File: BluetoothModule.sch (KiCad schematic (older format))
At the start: 13 parts, among them U2 BM83SM1-00TA

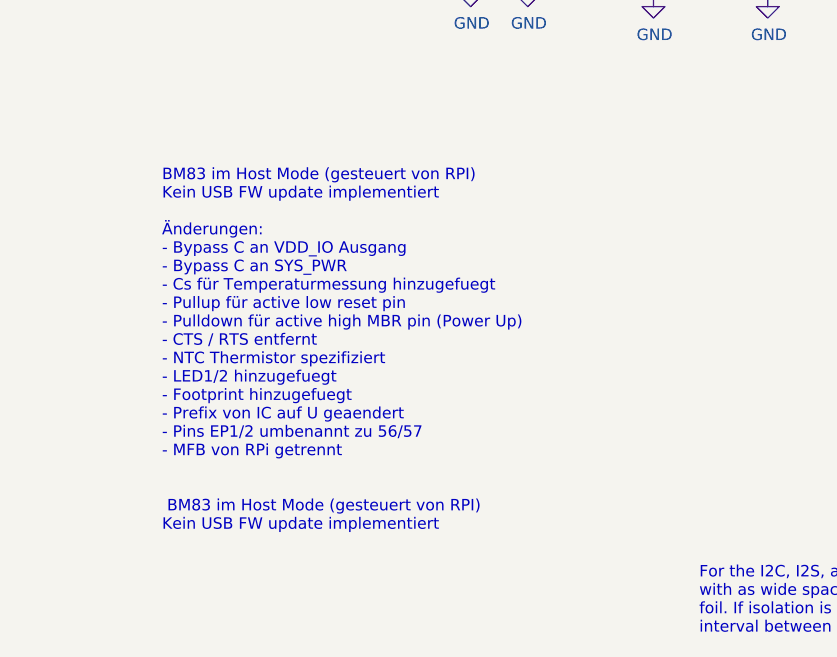
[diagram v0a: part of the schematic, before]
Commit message: - Erster Stand UI Board Layout
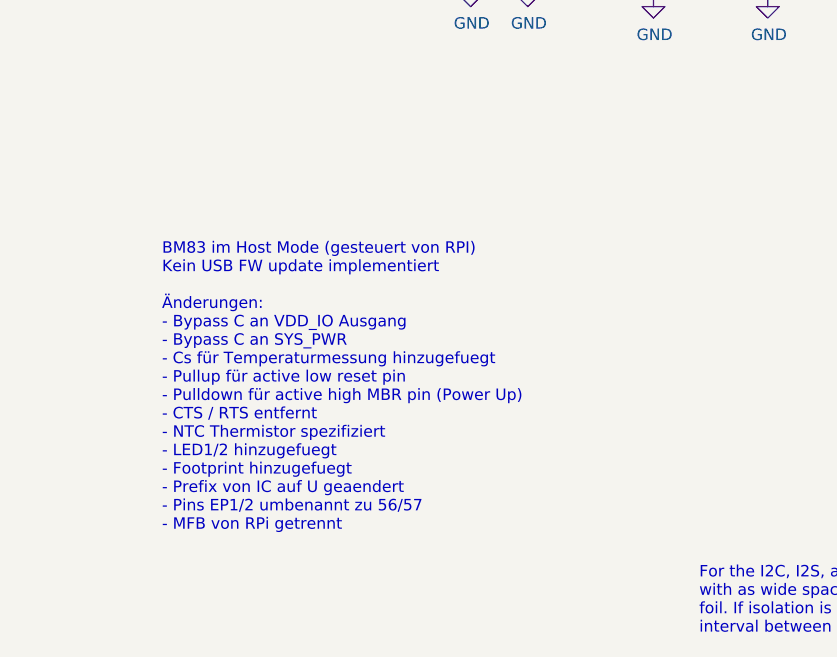
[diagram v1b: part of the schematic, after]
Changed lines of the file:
@@
 	6600 3850 6600 3950
 Text Notes 1050 7150 0    50   ~ 0
-BM83 im Host Mode (gesteuert von RPI)\nKein USB FW update implementiert\n\nÄnderungen:\n- Bypass C an VDD_IO Ausgang\n- Bypass C an SYS_PWR\n- Cs für Temperaturmessung hinzugefuegt\n- Pullup für active low reset pin\n- Pulldown für active high MBR pin (Power Up)\n- CTS / RTS entfernt\n- NTC Thermistor spezifiziert\n- LED1/2 hinzugefuegt\n- Footprint hinzugefuegt\n- Prefix von IC auf U geaendert\n- Pins EP1/2 umbenannt zu 56/57 \n- MFB von RPi getrennt\n\n\n BM83 im Host Mode (gesteuert von RPI)\nKein USB FW update implementiert
+BM83 im Host Mode (gesteuert von RPI)\nKein USB FW update implementiert\n\nÄnderungen:\n- Bypass C an VDD_IO Ausgang\n- Bypass C an SYS_PWR\n- Cs für Temperaturmessung hinzugefuegt\n- Pullup für active low reset pin\n- Pulldown für active high MBR pin (Power Up)\n- CTS / RTS entfernt\n- NTC Thermistor spezifiziert\n- LED1/2 hinzugefuegt\n- Footprint hinzugefuegt\n- Prefix von IC auf U geaendert\n- Pins EP1/2 umbenannt zu 56/57 \n- MFB von RPi getrennt
 $Bitmap
 Pos 5150 6250

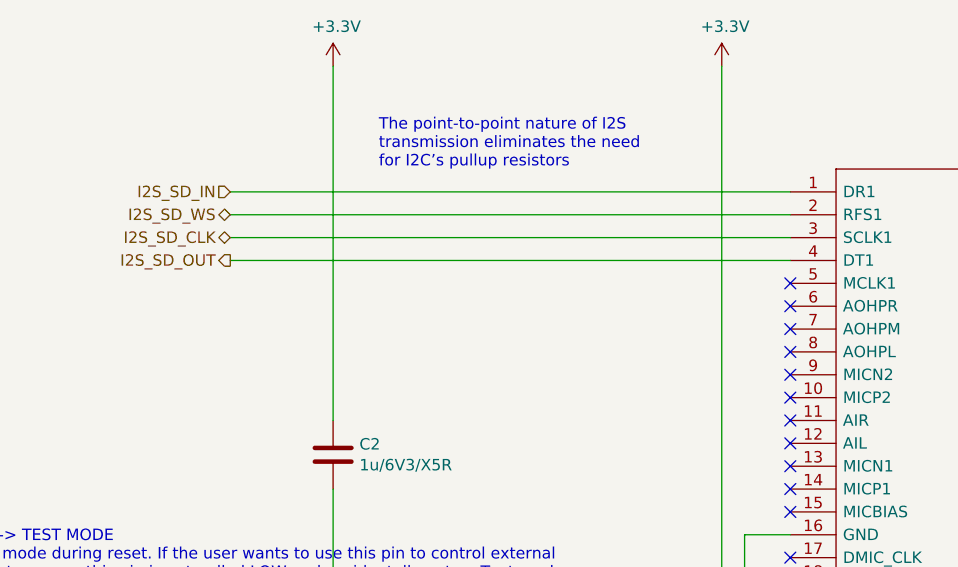
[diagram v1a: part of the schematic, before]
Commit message: [mod:] MCLK input to MAX98089 from BM83 at 12.28MHz
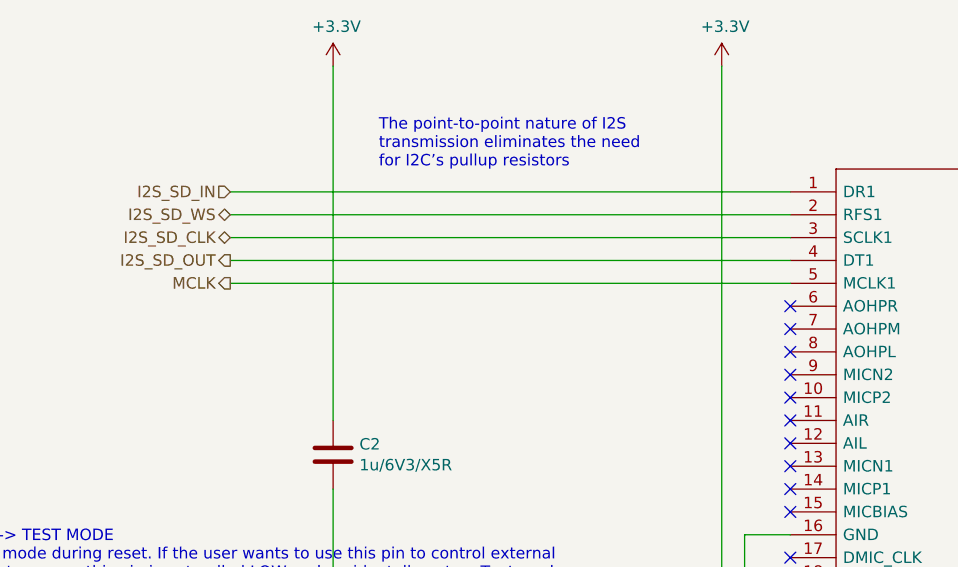
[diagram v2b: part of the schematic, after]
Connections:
- net MCLK: now reaches U2.5 (MCLK1)
- no-connect marks 34 -> 33
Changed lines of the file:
@@
 Text Notes 3400 7600 0    50   ~ 0
 For the I2C, I2S, and UART groups, each respective group's traces should run parallel\nwith as wide spacing as possible and be isolated from other groups with GND copper\nfoil. If isolation is not possible due to limited space, please at least increase the \ninterval between traces belonging to different groups.
-NoConn ~ 4400 1850
 Text Notes 7000 6350 0    50   ~ 0
 Wird das Modul als I2S Master betrieben, kann dessen MCLK Ausgang zur Frequenzversorgung \ndes Slaves verwendet werden. Dies ist hier aber nicht der Fall, daher bleibt MCLK unbeschalten.\nvgl. DS 6.5. Vermutlich könnte das Modul den MAX98089 mit dem Takt versorgen, \nso dass der Oszillator für MAX98 entfallen kann\n\nThe BM83 serves as a master to provide clock and frame synchronous signals for the master/slave data\nsynchronizations, as illustrated in the following figures. The MCLK is optional and is not required if the\nexternal I2S device can drive its system clock on its own.\n\nMaster CLK is not part of the I2S standard, but is commonly included for synchronizing \nthe internal operation of the analog/digital converters.\nQuelle: https://en.wikipedia.org/wiki/I%C2%B2S
@@
 	1    0    0    -1
 $EndComp
+Text HLabel 1950 1850 0    50   Output ~ 0
+MCLK
+Wire Wire Line
+	1950 1850 4400 1850
 $EndSCHEMATC

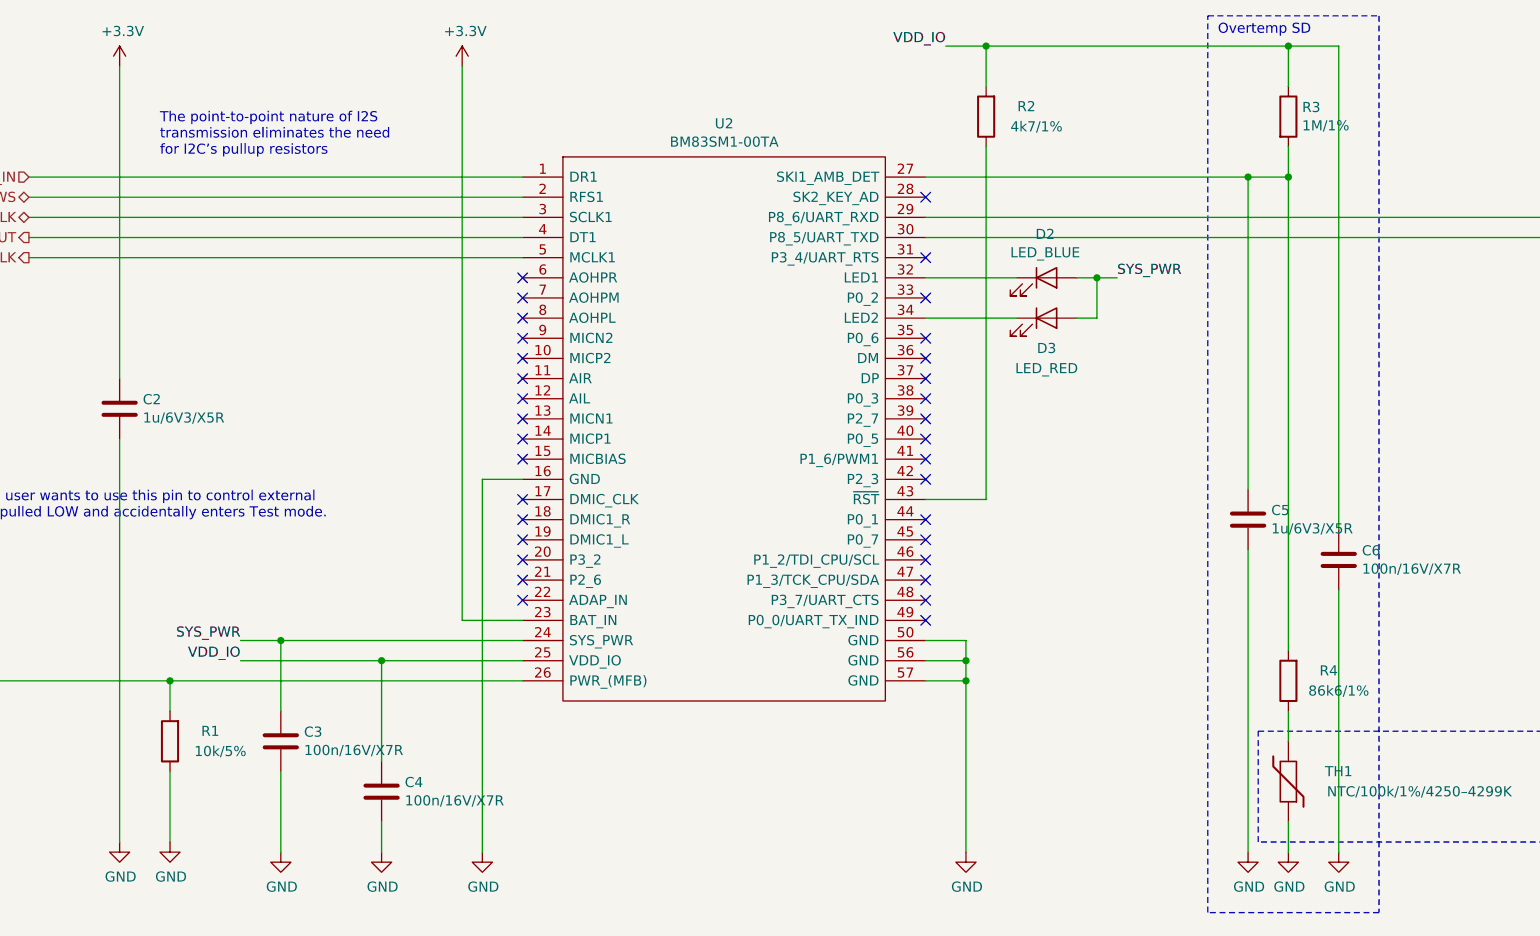
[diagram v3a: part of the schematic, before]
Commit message: - Schaltbare BL Versorgung fertig - kleinere Value Anpassungen - Finale Annotation
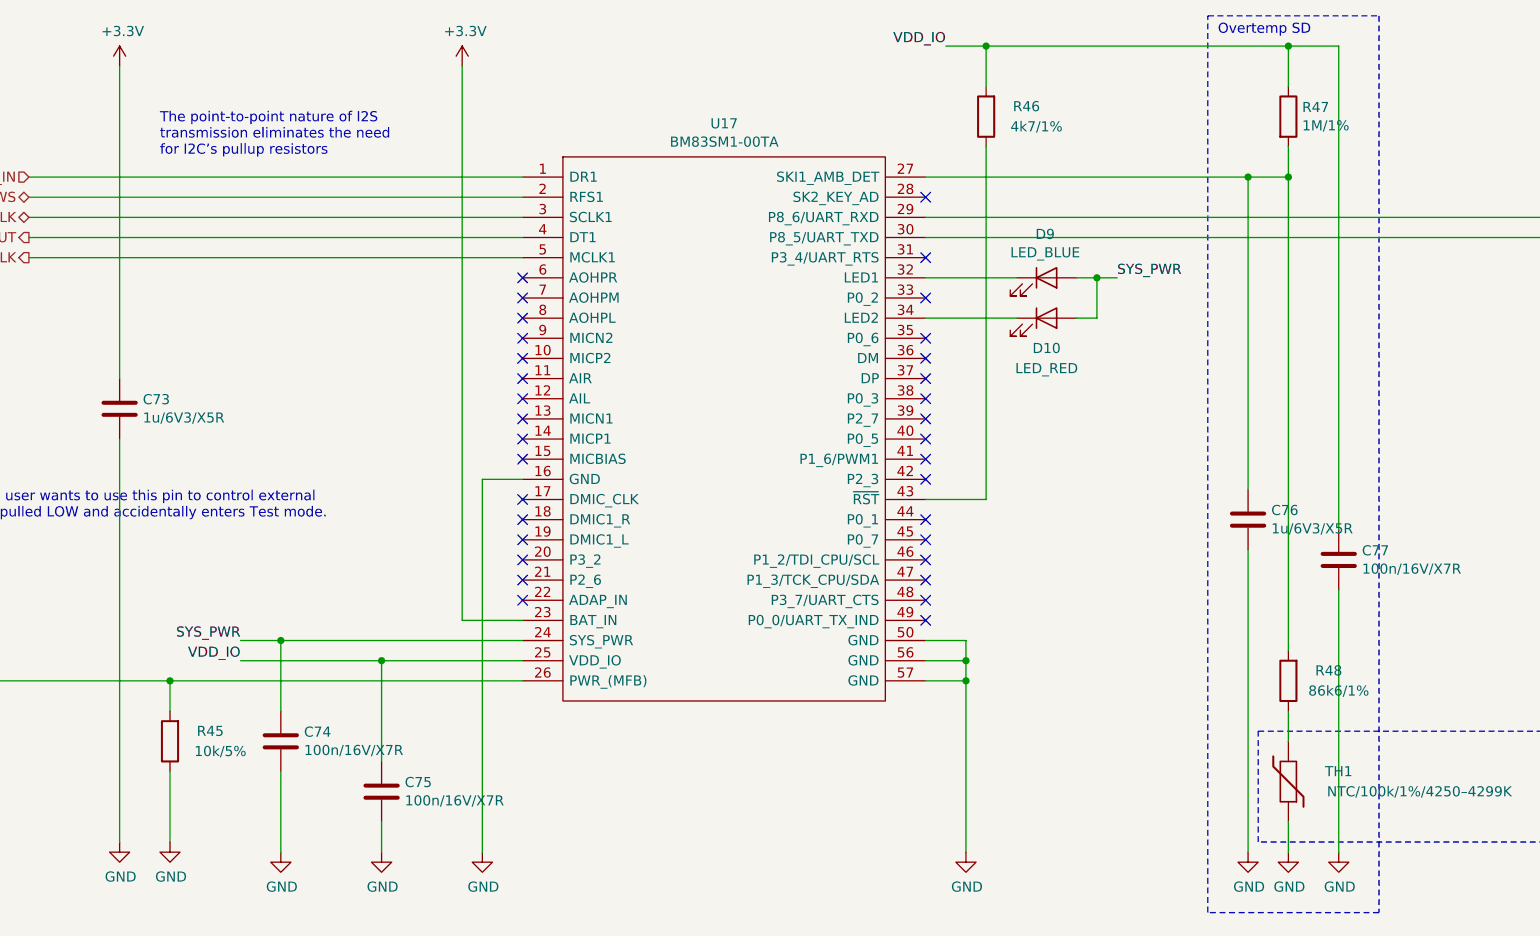
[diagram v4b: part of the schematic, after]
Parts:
- renumbered C2 to C73, C3 to C74, C4 to C75, C5 to C76, C6 to C77, D3 to D10, D2 to D9, R1 to R45, R2 to R46, R3 to R47, R4 to R48, U2 to U17
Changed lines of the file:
@@
 $EndDescr
 $Comp
-L TeKaDe:BM83SM1-00TA U2
+L TeKaDe:BM83SM1-00TA U17
 U 1 1 620D3641
 P 4400 1450
-F 0 "U2" H 5400 1715 50  0000 C CNN
+F 0 "U17" H 5400 1715 50  0000 C CNN
 F 1 "BM83SM1-00TA" H 5400 1624 50  0000 C CNN
 F 2 "TeKaDe:BM83SM1" H 6250 1550 50  0001 L CNN
@@
 NoConn ~ 4400 3550
 $Comp
-L power:+3.3V #PWR013
+L power:+3.3V #PWR0173
 U 1 1 620D3663
 P 4100 900
-F 0 "#PWR013" H 4100 750 50  0001 C CNN
+F 0 "#PWR0173" H 4100 750 50  0001 C CNN
 F 1 "+3.3V" H 4115 1073 50  0000 C CNN
 F 2 "" H 4100 900 50  0001 C CNN
@@
 $EndComp
 $Comp
-L Device:C C2
+L Device:C C73
 U 1 1 620D366F
 P 2400 2600
-F 0 "C2" H 2515 2646 50  0000 L CNN
+F 0 "C73" H 2515 2646 50  0000 L CNN
 F 1 "1u/6V3/X5R" H 2515 2555 50  0000 L CNN
 F 2 "Capacitor_SMD:C_0402_1005Metric" H 2438 2450 50  0001 C CNN
@@
 NoConn ~ 6400 3650
 $Comp
-L power:GND #PWR014
+L power:GND #PWR0174
 U 1 1 620E43D7
 P 4200 4800
-F 0 "#PWR014" H 4200 4550 50  0001 C CNN
+F 0 "#PWR0174" H 4200 4550 50  0001 C CNN
 F 1 "GND" H 4205 4627 50  0000 C CNN
 F 2 "" H 4200 4800 50  0001 C CNN
@@
 	4200 2950 4400 2950
 $Comp
-L power:GND #PWR015
+L power:GND #PWR0175
 U 1 1 620E7F5A
 P 6600 4800
-F 0 "#PWR015" H 6600 4550 50  0001 C CNN
+F 0 "#PWR0175" H 6600 4550 50  0001 C CNN
 F 1 "GND" H 6605 4627 50  0000 C CNN
 F 2 "" H 6600 4800 50  0001 C CNN
@@
 $EndComp
 $Comp
-L power:GND #PWR09
+L power:GND #PWR0169
 U 1 1 620F327C
 P 2400 4750
-F 0 "#PWR09" H 2400 4500 50  0001 C CNN
+F 0 "#PWR0169" H 2400 4500 50  0001 C CNN
 F 1 "GND" H 2405 4577 50  0000 C CNN
 F 2 "" H 2400 4750 50  0001 C CNN
@@
 	2400 4750 2400 2750
 $Comp
-L power:+3.3V #PWR08
+L power:+3.3V #PWR0168
 U 1 1 620F6127
 P 2400 900
-F 0 "#PWR08" H 2400 750 50  0001 C CNN
+F 0 "#PWR0168" H 2400 750 50  0001 C CNN
 F 1 "+3.3V" H 2415 1073 50  0000 C CNN
 F 2 "" H 2400 900 50  0001 C CNN
@@
 $EndBitmap
 $Comp
-L Device:C C4
+L Device:C C75
 U 1 1 60DA1121
 P 3700 4500
-F 0 "C4" H 3815 4546 50  0000 L CNN
+F 0 "C75" H 3815 4546 50  0000 L CNN
 F 1 "100n/16V/X7R" H 3815 4455 50  0000 L CNN
 F 2 "Capacitor_SMD:C_0402_1005Metric" H 3738 4350 50  0001 C CNN
@@
 $EndComp
 $Comp
-L power:GND #PWR012
+L power:GND #PWR0172
 U 1 1 60DA112B
 P 3700 4800
-F 0 "#PWR012" H 3700 4550 50  0001 C CNN
+F 0 "#PWR0172" H 3700 4550 50  0001 C CNN
 F 1 "GND" H 3705 4627 50  0000 C CNN
 F 2 "" H 3700 4800 50  0001 C CNN
@@
 	3700 3850 3700 4350
 $Comp
-L power:GND #PWR011
+L power:GND #PWR0171
 U 1 1 60DA7A97
 P 3200 4800
-F 0 "#PWR011" H 3200 4550 50  0001 C CNN
+F 0 "#PWR0171" H 3200 4550 50  0001 C CNN
 F 1 "GND" H 3205 4627 50  0000 C CNN
 F 2 "" H 3200 4800 50  0001 C CNN
@@
 Wird das Modul als I2S Master betrieben, kann dessen MCLK Ausgang zur Frequenzversorgung \ndes Slaves verwendet werden. Dies ist hier aber nicht der Fall, daher bleibt MCLK unbeschalten.\nvgl. DS 6.5. Vermutlich könnte das Modul den MAX98089 mit dem Takt versorgen, \nso dass der Oszillator für MAX98 entfallen kann\n\nThe BM83 serves as a master to provide clock and frame synchronous signals for the master/slave data\nsynchronizations, as illustrated in the following figures. The MCLK is optional and is not required if the\nexternal I2S device can drive its system clock on its own.\n\nMaster CLK is not part of the I2S standard, but is commonly included for synchronizing \nthe internal operation of the analog/digital converters.\nQuelle: https://en.wikipedia.org/wiki/I%C2%B2S
 $Comp
-L Device:R R2
+L Device:R R46
 U 1 1 60DB214B
 P 6700 1150
-F 0 "R2" H 6500 1100 50  0000 C CNN
+F 0 "R46" H 6500 1100 50  0000 C CNN
 F 1 "4k7/1%" H 6450 1200 50  0000 C CNN
 F 2 "Resistor_SMD:R_0402_1005Metric" V 6740 1140 50  0001 C CNN
@@
 Connection ~ 8000 1450
 $Comp
-L power:GND #PWR018
+L power:GND #PWR0178
 U 1 1 60DAF699
 P 8450 4800
-F 0 "#PWR018" H 8450 4550 50  0001 C CNN
+F 0 "#PWR0178" H 8450 4550 50  0001 C CNN
 F 1 "GND" H 8455 4627 50  0000 C CNN
 F 2 "" H 8450 4800 50  0001 C CNN
@@
 $EndComp
 $Comp
-L power:GND #PWR016
+L power:GND #PWR0176
 U 1 1 60DAEFE7
 P 8000 4800
-F 0 "#PWR016" H 8000 4550 50  0001 C CNN
+F 0 "#PWR0176" H 8000 4550 50  0001 C CNN
 F 1 "GND" H 8005 4627 50  0000 C CNN
 F 2 "" H 8000 4800 50  0001 C CNN
@@
 $EndComp
 $Comp
-L Device:C C5
+L Device:C C76
 U 1 1 60DAD2BA
 P 8000 3150
-F 0 "C5" H 8115 3196 50  0000 L CNN
+F 0 "C76" H 8115 3196 50  0000 L CNN
 F 1 "1u/6V3/X5R" H 8115 3105 50  0000 L CNN
 F 2 "Capacitor_SMD:C_0402_1005Metric" H 8038 3000 50  0001 C CNN
@@
 	8200 1450 8200 3800
 $Comp
-L power:GND #PWR017
+L power:GND #PWR0177
 U 1 1 60E2C9E3
 P 8200 4800
-F 0 "#PWR017" H 8200 4550 50  0001 C CNN
+F 0 "#PWR0177" H 8200 4550 50  0001 C CNN
 F 1 "GND" H 8205 4627 50  0000 C CNN
 F 2 "" H 8200 4800 50  0001 C CNN
@@
 $EndComp
 $Comp
-L Device:R R4
+L Device:R R48
 U 1 1 620D36B1
 P 8200 3950
-F 0 "R4" H 8000 3900 50  0000 C CNN
+F 0 "R48" H 8000 3900 50  0000 C CNN
 F 1 "86k6/1%" H 7950 4000 50  0000 C CNN
 F 2 "Resistor_SMD:R_0402_1005Metric" V 8240 3940 50  0001 C CNN
@@
 	8200 1300 8200 1450
 $Comp
-L Device:R R3
+L Device:R R47
 U 1 1 620D36AB
 P 8200 1150
-F 0 "R3" H 8268 1196 50  0000 L CNN
+F 0 "R47" H 8268 1196 50  0000 L CNN
 F 1 "1M/1%" H 8268 1105 50  0000 L CNN
 F 2 "Resistor_SMD:R_0402_1005Metric" V 8240 1140 50  0001 C CNN
@@
 	8450 3200 8450 800
 $Comp
-L Device:R R1
+L Device:R R45
 U 1 1 60E6FDE1
 P 2650 4250
-F 0 "R1" H 2450 4200 50  0000 C CNN
+F 0 "R45" H 2450 4200 50  0000 C CNN
 F 1 "10k/5%" H 2400 4300 50  0000 C CNN
 F 2 "Resistor_SMD:R_0402_1005Metric" V 2690 4240 50  0001 C CNN
@@
 $EndComp
 $Comp
-L power:GND #PWR010
+L power:GND #PWR0170
 U 1 1 60E7094B
 P 2650 4750
-F 0 "#PWR010" H 2650 4500 50  0001 C CNN
+F 0 "#PWR0170" H 2650 4500 50  0001 C CNN
 F 1 "GND" H 2655 4577 50  0000 C CNN
 F 2 "" H 2650 4750 50  0001 C CNN
@@
 SYS_PWR
 $Comp
-L Device:LED D2
+L Device:LED D9
 U 1 1 60E96C02
 P 7000 1950
-F 0 "D2" H 6993 2166 50  0000 C CNN
+F 0 "D9" H 6993 2166 50  0000 C CNN
 F 1 "LED_BLUE" H 6993 2075 50  0000 C CNN
 F 2 "LED_SMD:LED_0603_1608Metric" H 7000 1950 50  0001 C CNN
@@
 Connection ~ 6700 800
 $Comp
-L Device:LED D3
+L Device:LED D10
 U 1 1 60EA3694
 P 7000 2150
-F 0 "D3" H 7000 2000 50  0000 C CNN
+F 0 "D10" H 7000 2000 50  0000 C CNN
 F 1 "LED_RED" H 7000 1900 50  0000 C CNN
 F 2 "LED_SMD:LED_0603_1608Metric" H 7000 2150 50  0001 C CNN
@@
 	1950 1650 4400 1650
 $Comp
-L Device:C C3
+L Device:C C74
 U 1 1 60F92DF8
 P 3200 4250
-F 0 "C3" H 3315 4296 50  0000 L CNN
+F 0 "C74" H 3315 4296 50  0000 L CNN
 F 1 "100n/16V/X7R" H 3315 4205 50  0000 L CNN
 F 2 "Capacitor_SMD:C_0402_1005Metric" H 3238 4100 50  0001 C CNN
@@
 $EndComp
 $Comp
-L Device:C C6
+L Device:C C77
 U 1 1 60F9332A
 P 8450 3350
-F 0 "C6" H 8565 3396 50  0000 L CNN
+F 0 "C77" H 8565 3396 50  0000 L CNN
 F 1 "100n/16V/X7R" H 8565 3305 50  0000 L CNN
 F 2 "Capacitor_SMD:C_0402_1005Metric" H 8488 3200 50  0001 C CNN

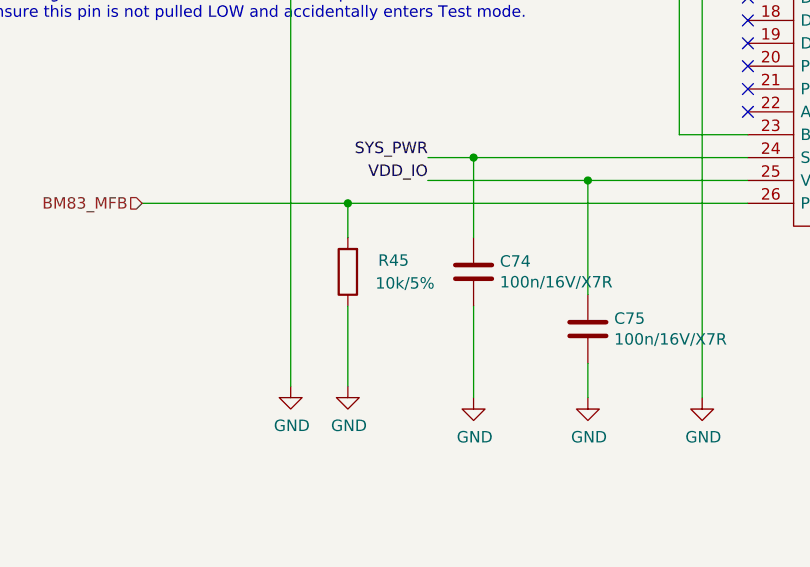
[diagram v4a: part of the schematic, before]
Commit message: - Bauteile konsolidiert
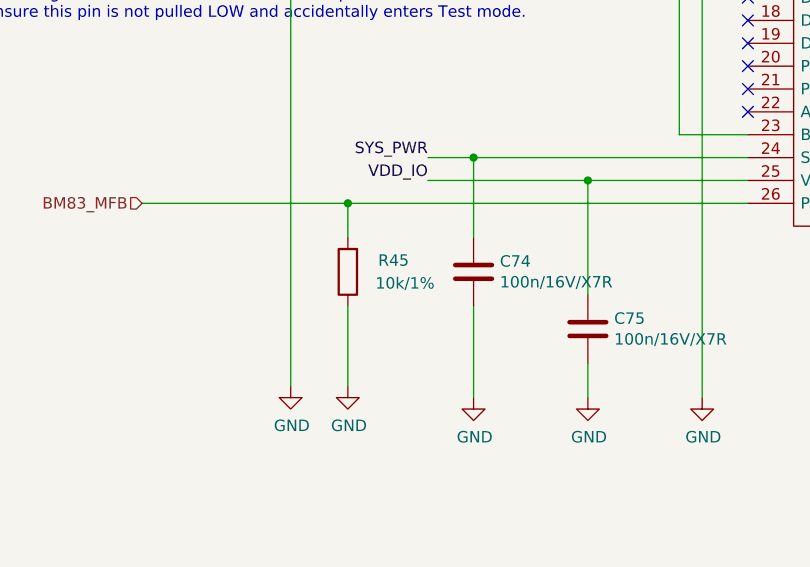
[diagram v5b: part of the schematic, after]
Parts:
- R45: value 10k/5% -> 10k/1%
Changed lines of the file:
@@
 P 2650 4250
 F 0 "R45" H 2450 4200 50  0000 C CNN
-F 1 "10k/5%" H 2400 4300 50  0000 C CNN
+F 1 "10k/1%" H 2400 4300 50  0000 C CNN
 F 2 "Resistor_SMD:R_0402_1005Metric" V 2690 4240 50  0001 C CNN
 F 3 "~" H 2650 4250 50  0001 C CNN
